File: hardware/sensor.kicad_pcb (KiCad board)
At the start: 2 copper layers, 56 parts, among them P1 CONN_01X05, SW1 Reset, T1 BUK9Y22, U1 LMR16006, U2 CD74HC4046, U3 CD74HC4046, U4 Atmel_SAM_D09, U5 OPA376AIDCK, X1 UART, X2 60V

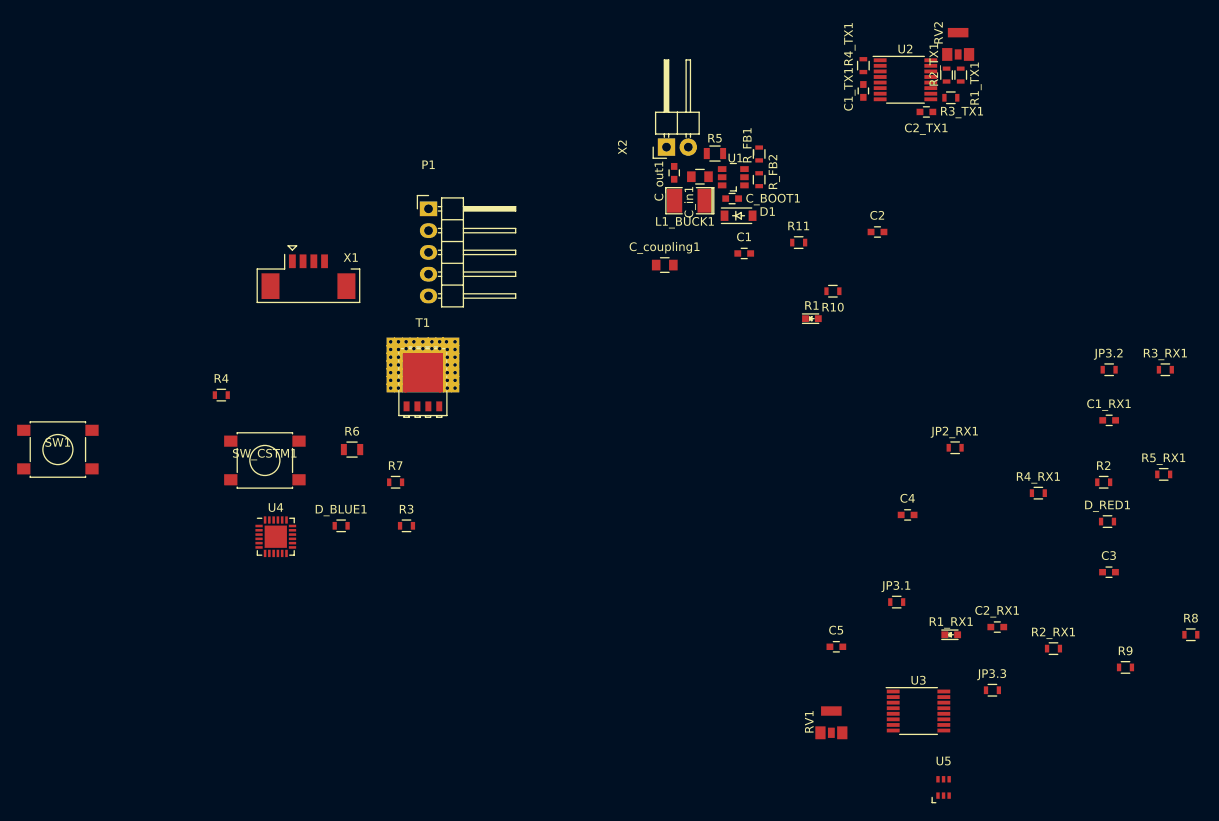
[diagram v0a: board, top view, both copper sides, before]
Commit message: Fixed some schematic mistakes and footprints. Continued placing parts.
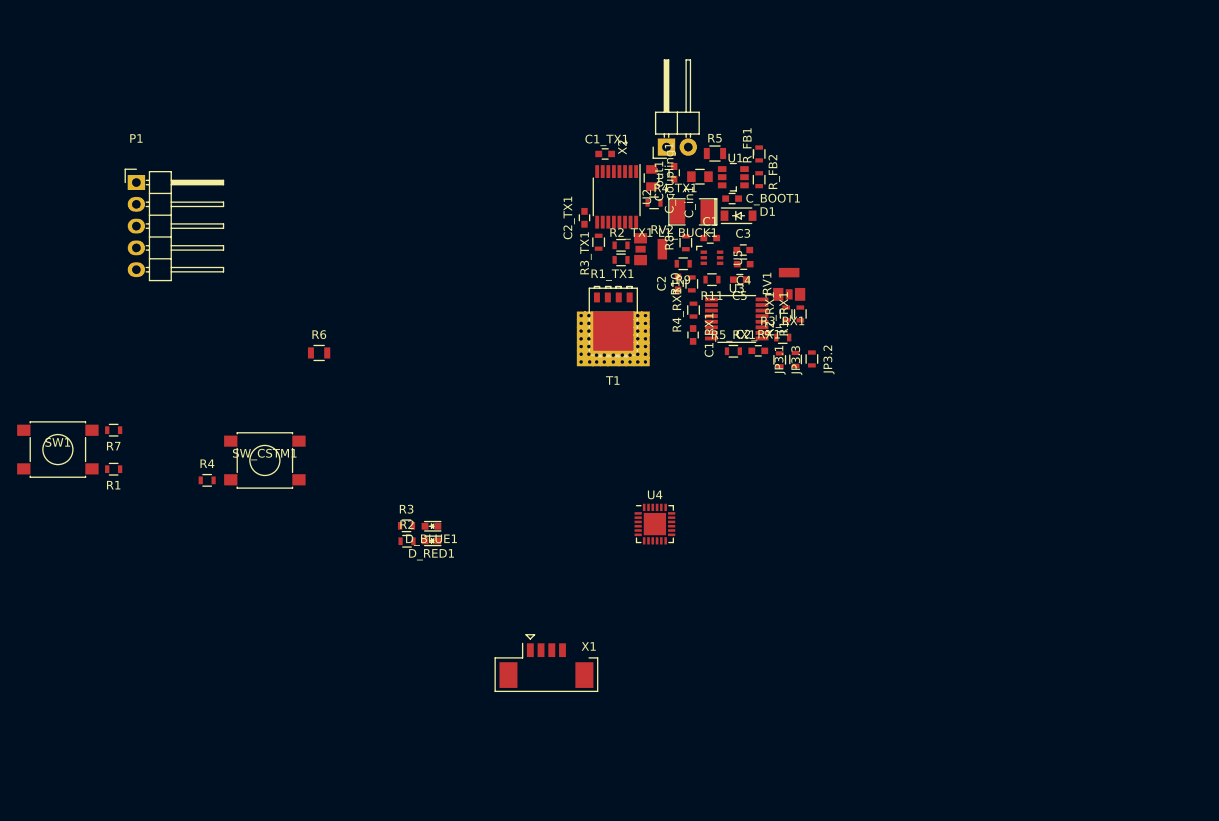
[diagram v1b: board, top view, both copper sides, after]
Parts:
- removed JP2_RX1: R_Small, Resistors_SMD:R_0603
- D_BLUE1, D_RED1: footprint Resistors_SMD:R_0603 -> LEDs:LED-0603
- R1, R1_RX1: footprint LEDs:LED_0603 -> Resistors_SMD:R_0603
- moved R1 83.3 mm to (95.4, 114.0), turned to 180 degrees
- moved R2 81.5 mm to (129.6, 122.5)
- moved D_RED1 78.8 mm to (132.5, 122.4), turned to 180 degrees
- moved R8 74.5 mm to (162.1, 87.7), turned to 90 degrees
- moved R9 69.8 mm to (161.8, 90.1), turned to 180 degrees
- moved U5 67.4 mm to (165.2, 89.4), turned to 270 degrees
- moved C3 56.8 mm to (168.8, 88.5)
- moved X1 53.2 mm to (145.8, 138.1)
- moved R5_RX1 52.2 mm to (167.7, 100.3)
- moved RV1 51.3 mm to (174.2, 92.4)
- moved U3 50.4 mm to (168.0, 96.5)
- moved R2_RX1 49.9 mm to (173.8, 96.0), turned to 90 degrees
- moved C1_RX1 49.5 mm to (162.9, 98.4), turned to 270 degrees
- moved JP3.3 45.8 mm to (173.1, 101.3), turned to 270 degrees
- moved R4_RX1 45.5 mm to (163.0, 95.5), turned to 90 degrees
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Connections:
- C1 pad 2: Net-(C1-Pad2) -> GND
- R3_RX1 pad 1: Net-(R3_RX1-Pad1) -> /VCOin
- U3 pad 4: Net-(JP2_RX1-Pad2) -> /JP2

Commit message: Finished placing for now
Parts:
- C1, C1_RX1, C2, C2_RX1, C2_TX1, C3, C4, C5, D_BLUE1, D_RED1, JP3.1, JP3.2, JP3.3, R10, R11, R1_RX1, R2, R2_RX1, R3, R3_RX1, R4_RX1, R5_RX1, R6, R7, R8, R9, RV1, SW1, SW_CSTM1, U3, U4, U5: moved to B.Cu
- P1: footprint Pin_Headers:Pin_Header_Angled_1x05 -> Connectors_Molex:Connector_Molex_PicoBlade_53261-0571
- R1: value R_Small -> 10k; moved to B.Cu
- moved SW1 80.8 mm to (168.9, 100.8), turned to 90 degrees
- moved R7 63.4 mm to (154.5, 86.5), turned to 0 degrees
- moved P1 63.1 mm to (159.8, 93.4), turned to 180 degrees
- moved R1 59.1 mm to (151.2, 94.6), turned to 90 degrees
- moved R4 58.6 mm to (161.9, 96.8)
- moved X1 52.9 mm to (170.6, 91.2), turned to 90 degrees
- moved SW_CSTM1 50.4 mm to (161.9, 100.8), turned to 270 degrees
- moved D_RED1 35.9 mm to (156.5, 95.8)
- moved D_BLUE1 35.9 mm to (156.5, 94.1)
- moved R3 35.8 mm to (153.6, 94.2)
- moved R2 35.8 mm to (153.6, 95.9)
- moved R6 35.2 mm to (151.7, 86.4)
- moved U4 30.3 mm to (154.8, 90.4), turned to 270 degrees
- moved C1_RX1 18.1 mm to (167.7, 80.9), turned to 0 degrees
- moved T1 15.9 mm to (153.0, 81.0), turned to 0 degrees
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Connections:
- R5_RX1 pad 2: /RX2_out -> /RX1_out
- U3 pad 10: /RX2_out -> /RX1_out
- U4 pad 22: /RX_in -> /RX1_out
- U4 pad 25: (no net) -> GND

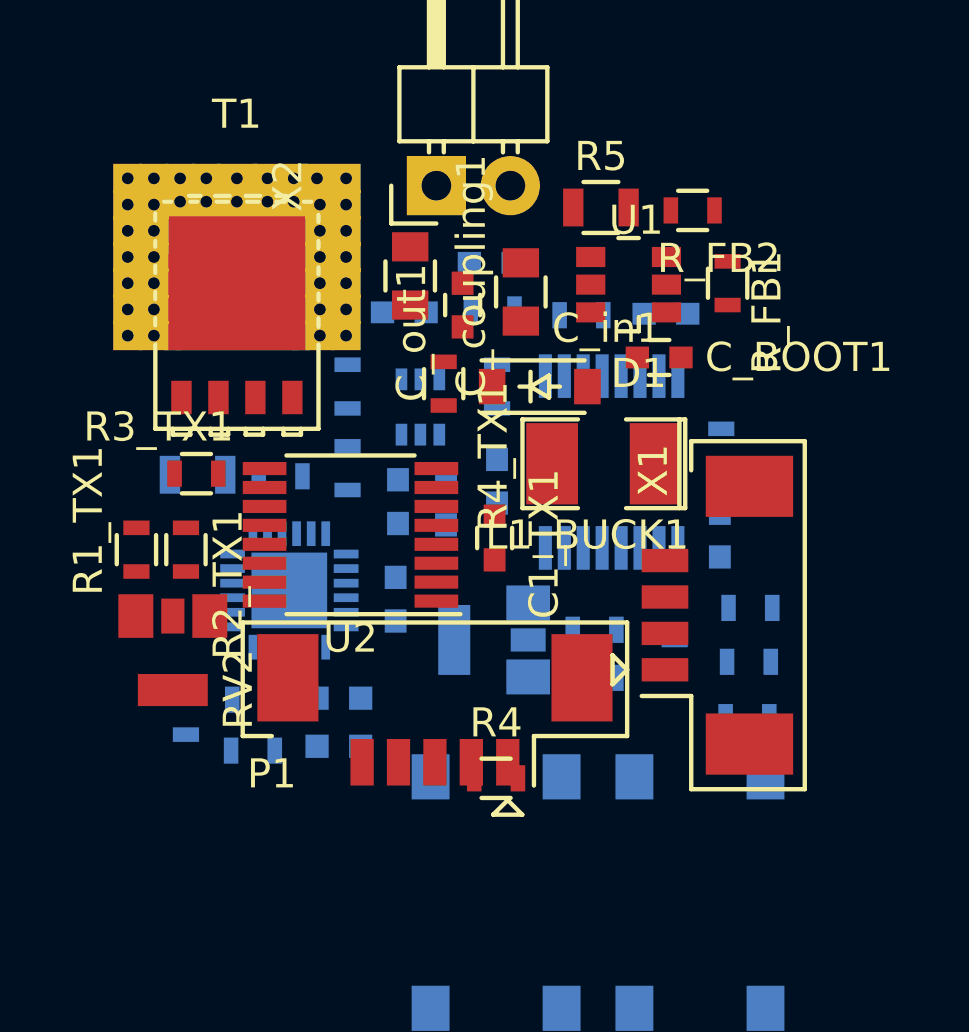
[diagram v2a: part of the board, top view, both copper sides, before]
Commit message: Routing started. VCC and GND still need routing. Probably need to lower density of parts for a proper groundplane ...
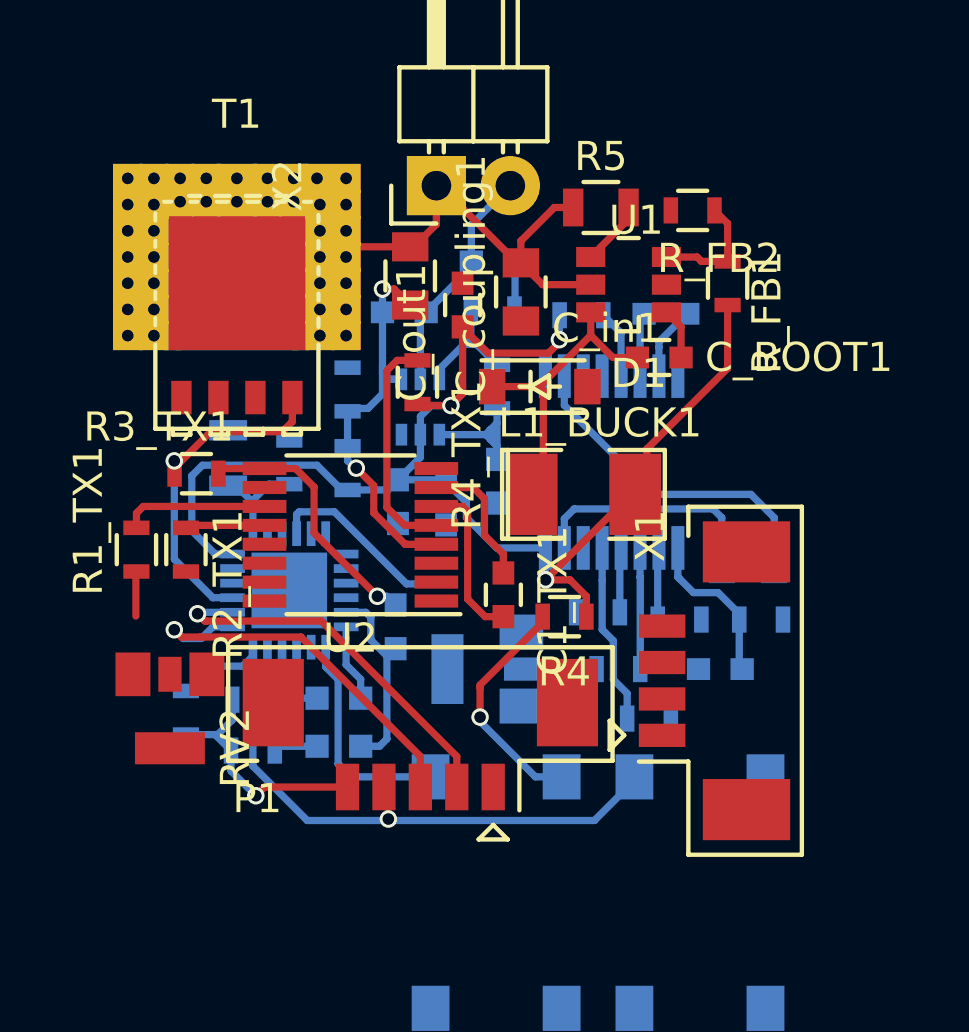
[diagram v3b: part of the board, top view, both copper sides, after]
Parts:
- moved R4 6.03 mm to (164.2, 91.3), turned to 180 degrees
- moved R5_RX1 5.97 mm to (168.2, 91.4), turned to 180 degrees
- moved C2_RX1 4.60 mm to (169.6, 93.1), turned to 180 degrees
- moved JP3.1 3.80 mm to (171.4, 89.2), turned to 270 degrees
- moved JP3.2 3.38 mm to (167.2, 94.8), turned to 180 degrees
- moved R3_RX1 2.97 mm to (171.0, 91.4), turned to 180 degrees
- moved X1 2.25 mm to (170.5, 93.5)
- moved JP3.3 2.09 mm to (169.7, 89.2), turned to 90 degrees
- moved RV2 2.00 mm to (150.7, 94.5)
- moved C1_TX1 1.97 mm to (162.2, 90.5)
- moved L1_BUCK1 1.26 mm to (164.9, 87.1), turned to 0 degrees
- moved R6 1.20 mm to (152.7, 85.8), turned to 270 degrees
- moved RV1 1.03 mm to (161.5, 93.1)
- moved P1 0.99 mm to (159.3, 94.2)
- moved C2_TX1 0.95 mm to (158.4, 91.7)
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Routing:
- net +3V3: track 0.00 -> 54.1 mm, vias 0 -> 4
- net VCC: track 0.00 -> 50.8 mm
- net Net-(P1-Pad4): track 0.00 -> 23.4 mm, vias 0 -> 1
- net /coupling: track 0.00 -> 14.5 mm, vias 0 -> 2
- net Net-(P1-Pad3): track 0.00 -> 13.6 mm, vias 0 -> 1
- net Net-(P1-Pad2): track 0.00 -> 13.2 mm, vias 0 -> 1
- net GND: track 0.00 -> 12.9 mm
- net Net-(JP3.1-Pad1): track 0.00 -> 10.3 mm
- net Net-(C_BOOT1-Pad2): track 0.00 -> 9.52 mm
- net Net-(C2_TX1-Pad1): track 0.00 -> 9.03 mm, vias 0 -> 1
- net /TX1_in: track 0.00 -> 8.70 mm, vias 0 -> 1
- net Net-(R4-Pad2): track 0.00 -> 8.08 mm, vias 0 -> 1
- net Net-(R4_TX1-Pad2): track 0.00 -> 7.85 mm
- net /SW_CSTM: track 0.00 -> 7.54 mm
- net Net-(JP3.3-Pad2): track 0.00 -> 7.17 mm
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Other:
- net class pro4_default added: clearance 0.25, trace_width 0.2, via_dia 0.7, via_drill 0.4

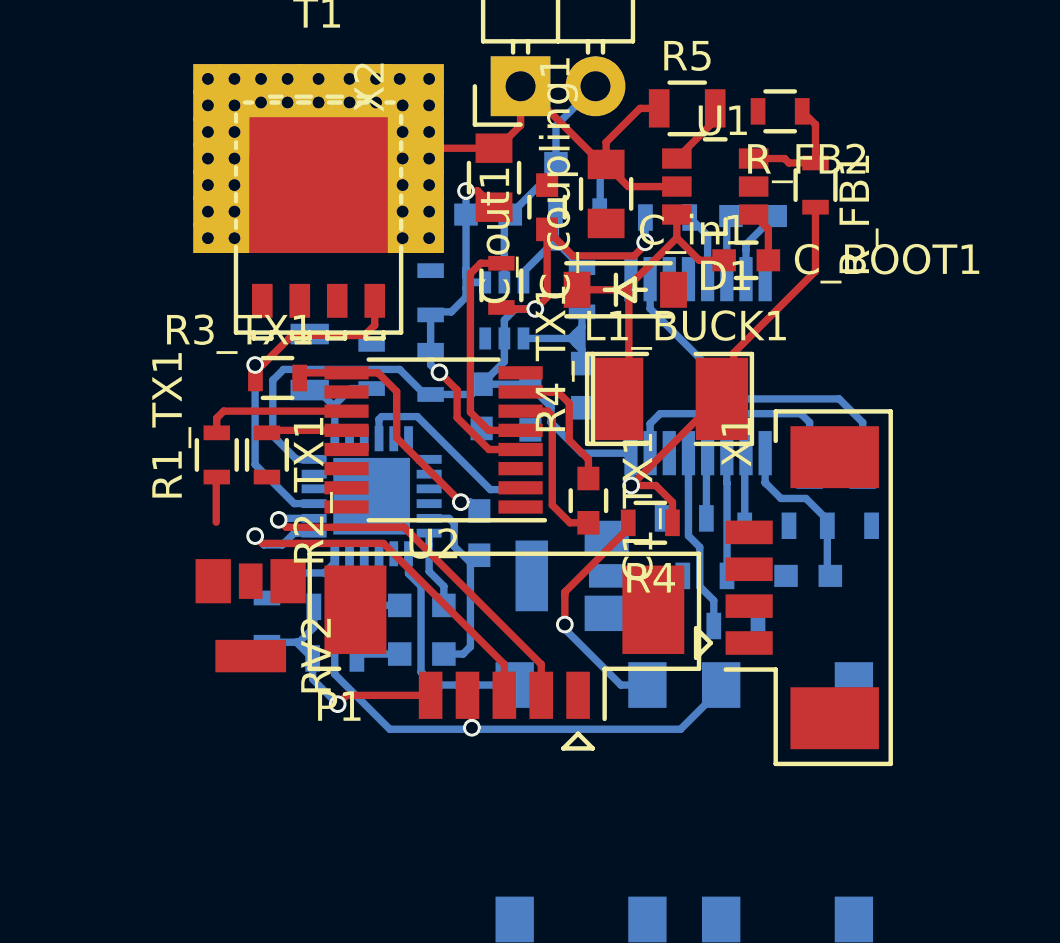
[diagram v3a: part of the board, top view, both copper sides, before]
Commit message: Finished routing except GND (needs plane etc pp); VCC and maybe even 3V3 needs thicker traces; Fixed missing supply cap for SAMD09 in the schema as well as some wrong footprint for SWD
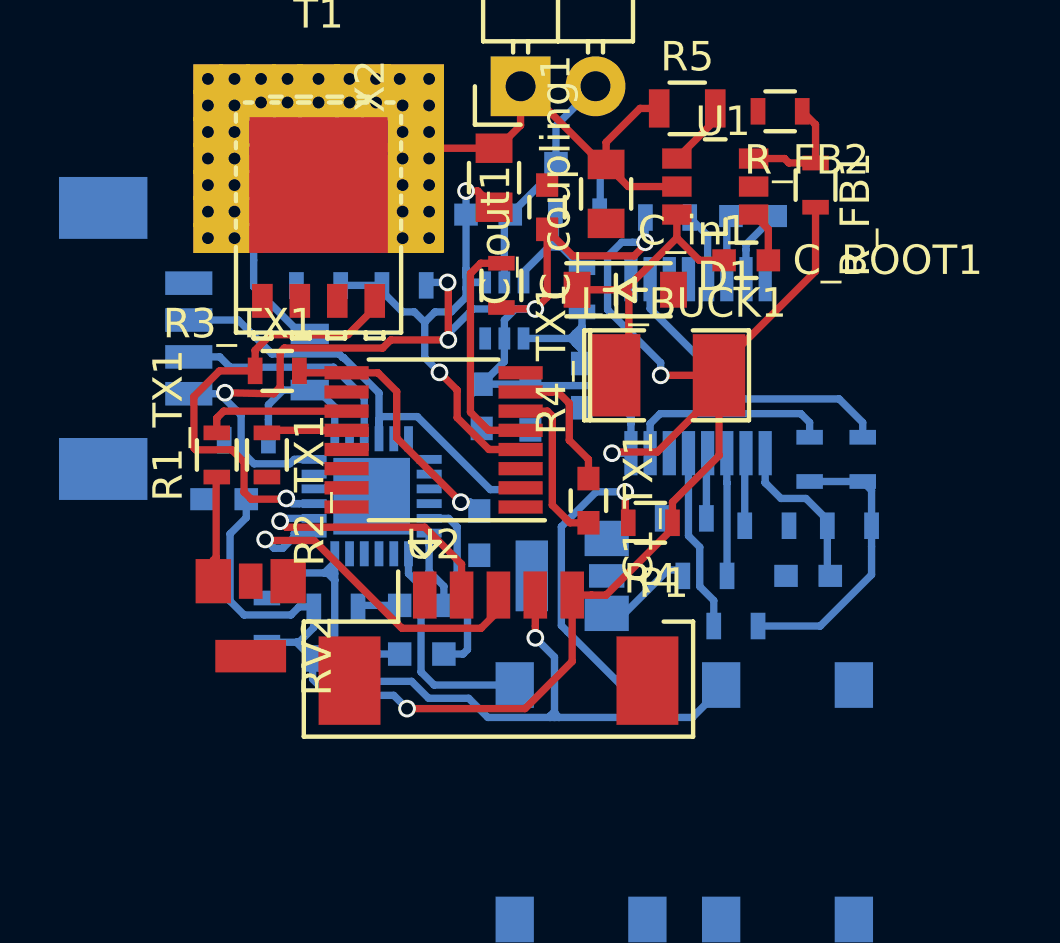
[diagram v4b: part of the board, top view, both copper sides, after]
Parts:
- added C6: 100n, Capacitors_SMD:C_0603, B.Cu at (149.8, 90.5)
- X1: moved to B.Cu
- moved X1 26.2 mm to (145.7, 85.0)
- moved R7 4.93 mm to (150.6, 88.5), turned to 180 degrees
- moved R9 3.81 mm to (153.0, 83.2), turned to 180 degrees
- moved R8 3.08 mm to (155.9, 83.2), turned to 180 degrees
- moved P1 2.41 mm to (159.1, 96.7), turned to 0 degrees
- moved L1_BUCK1 0.81 mm to (164.8, 86.3)
- moved R3_TX1 0.24 mm to (151.6, 86.2)
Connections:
- X1 pad 1: VCC -> +3V3
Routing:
- net +3V3: track 54.1 -> 95.1 mm, vias 4 -> 8
- net Net-(U4-Pad4): track 6.15 -> 15.2 mm
- net Net-(U4-Pad3): track 0.00 -> 7.91 mm
- net /VCOin: track 1.87 -> 9.73 mm
- net /TX1_in: track 8.70 -> 15.7 mm
- net GND: track 12.9 -> 7.93 mm
- net /RED_ON: track 1.32 -> 6.24 mm
- net Net-(P1-Pad2): track 13.2 -> 9.00 mm
- net /coupling: track 14.5 -> 18.1 mm
- net Net-(P1-Pad4): track 23.4 -> 26.8 mm
- net Net-(R4-Pad2): track 8.08 -> 11.1 mm
- net VCC: track 50.8 -> 53.2 mm
- net Net-(R1_TX1-Pad2): track 1.54 -> 3.58 mm
- net Net-(P1-Pad3): track 13.6 -> 12.2 mm
- net /adc_0: track 3.72 -> 4.97 mm
